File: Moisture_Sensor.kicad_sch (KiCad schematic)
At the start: 18 parts, among them J1 UPDI, J2 OLED SSD1306 0.96in, J3 STEMMA QT soil sensor, J4 Analog cap. sensor (alt), Q1 DMG3415U, SW1 READ, U1 ATtiny1614-SSNR, U2 TPS22917DBVR

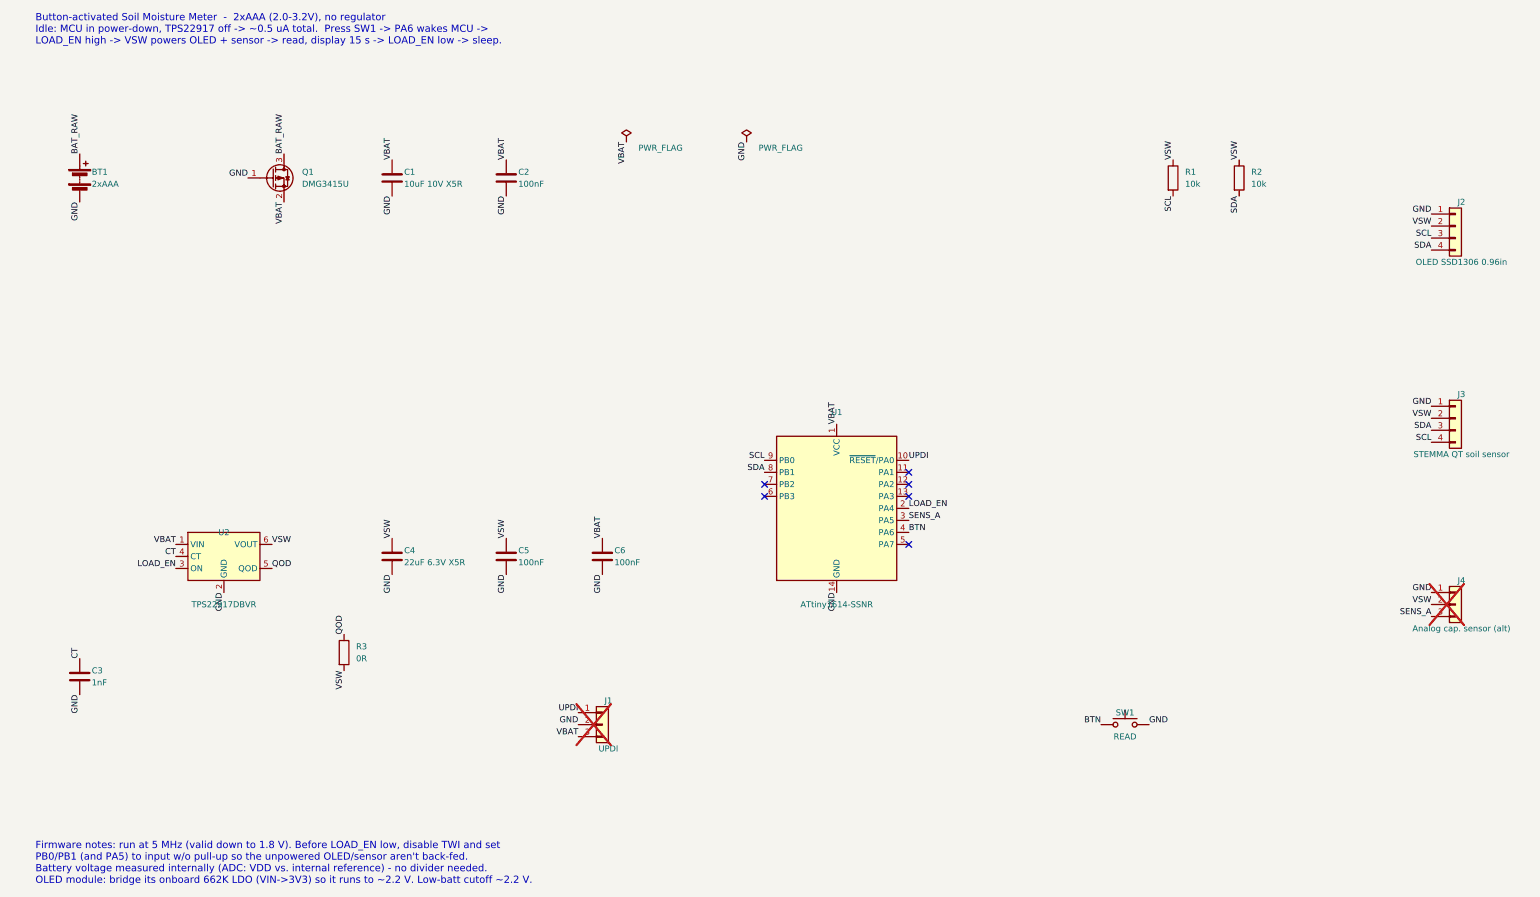
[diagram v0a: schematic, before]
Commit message: Add 25x17 mm PCB layout, STEP, renders; update schematic connectors
Co-authored-by: Copilot App <223556219+Copilot@users.noreply.github.com>
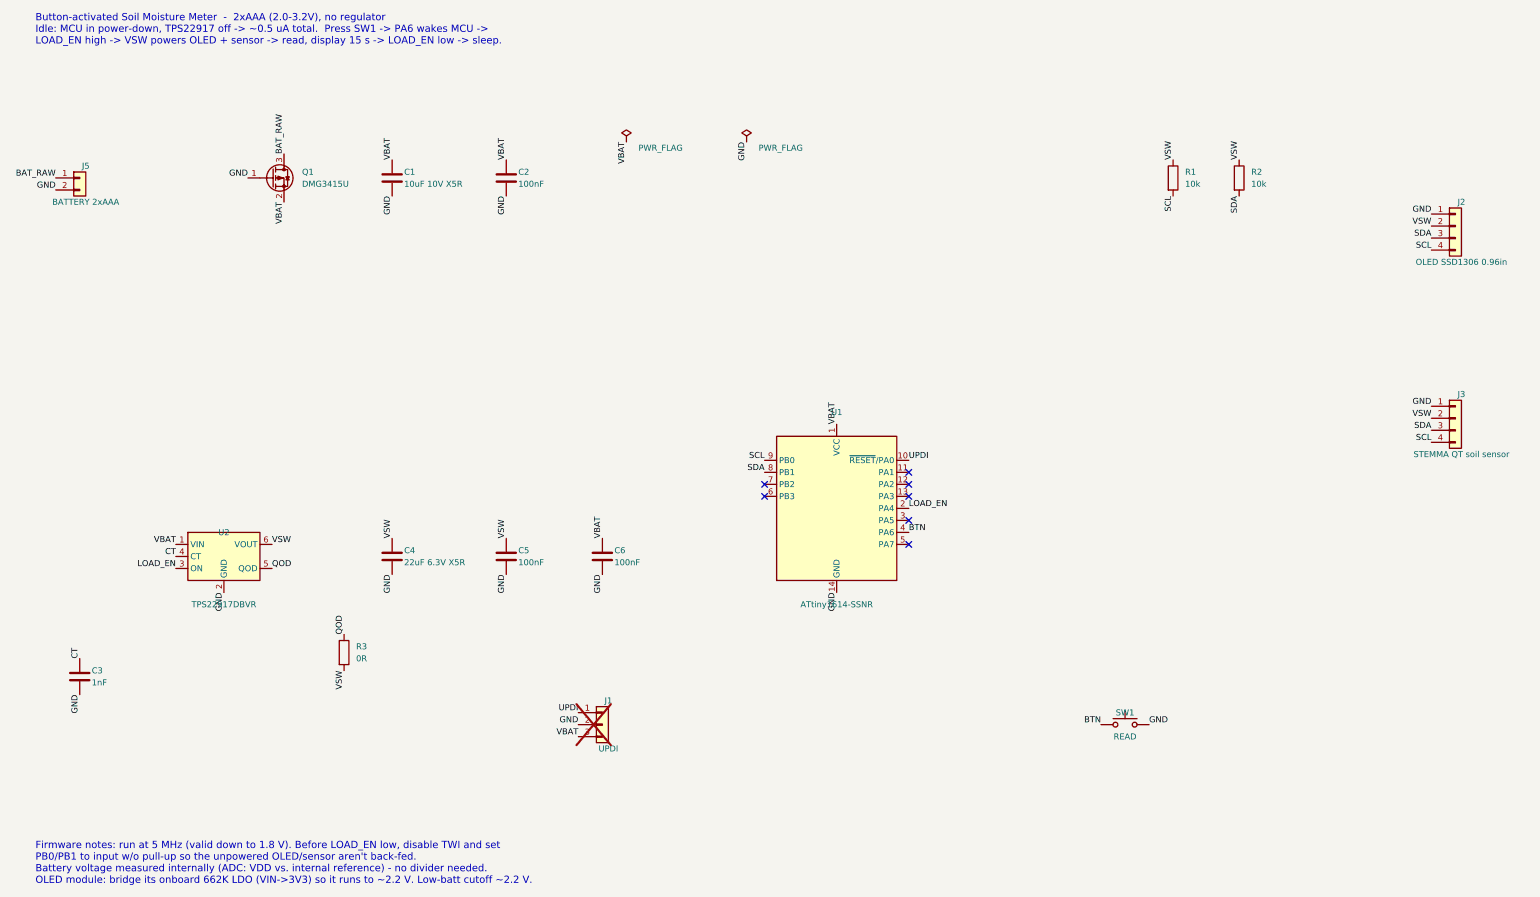
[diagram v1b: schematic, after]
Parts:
- removed BT1: 2xAAA, Battery:BatteryHolder_Keystone_2468_2xAAA, symbol Device:Battery
- removed J4: Analog cap. sensor (alt), Connector_JST:JST_PH_B3B-PH-K_1x03_P2.00mm_Vertical, symbol Connector_Generic:Conn_01x03
- added J5: BATTERY 2xAAA, Connector_JST:JST_PH_B2B-PH-K_1x02_P2.00mm_Vertical, symbol Connector_Generic:Conn_01x02
- J1: footprint Connector_PinHeader_2.54mm:PinHeader_1x03_P2.54mm_Vertical -> Connector_PinHeader_2.54mm:PinHeader_1x03_P2.54mm_Vertical_SMD_Pin1Left; Note Programming header (pogo pads / temporary header) -> UPDI programming pads on PCB bottom (pogo / temporary heade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
- J2: footprint Connector_PinHeader_2.54mm:PinHeader_1x04_P2.54mm_Vertical -> Connector_JST:JST_SH_SM04B-SRSS-TB_1x04-1MP_P1.00mm_Horizontal; MPN (none) -> SM04B-SRSS-TB(LF)(SN); Manufacturer (none) -> JST; Note ELEGOO 0.96in I2C OLED (GND,VCC,SCL,SDA) -> STEMMA QT pinout; cable e.g. Adafruit 4397 to OLED header
- SW1: footprint Button_Switch_THT:SW_PUSH_6mm -> Button_Switch_SMD:SW_Push_1P1T_NO_CK_KMR2; MPN B3F-1000 -> KMR221GLFS; Manufacturer Omron -> C&K
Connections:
- net BAT_RAW: now also J5.1 (Pin_1)
- net GND: now also J5.2 (Pin_2)
- net SCL: now also J2.4 (Pin_4); no longer J2.3 (Pin_3)
- net SDA: now also J2.3 (Pin_3); no longer J2.4 (Pin_4)
- net SENS_A: no longer names the net of U1.3 (PA5)
- no-connect marks 6 -> 7
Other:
- note added: "Firmware notes: run at 5 MHz (valid down to 1.8 V). Before LOAD_EN low, disable TWI and set PB0/PB1 to input w/o pull-up so the unpowered OLED/sensor aren't back-fed. Battery voltage measured internally (ADC: VDD vs. internal reference) - no divider needed. OLED module: bridge its onboard 662K LDO (VIN->3V3) so it runs to ~2.2 V. Low-batt cutoff ~2.2 V."
- note removed: "Firmware notes: run at 5 MHz (valid down to 1.8 V). Before LOAD_EN low, disable TWI and set PB0/PB1 (and PA5) to input w/o pull-up so the unpowered OLED/sensor aren't back-fed. Battery voltage measured internally (ADC: VDD vs. internal reference) - no divider needed. OLED module: bridge its onboard 662K LDO (VIN->3V3) so it runs to ~2.2 V. Low-batt cutoff ~2.2 V."
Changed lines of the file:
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@@
 	)
 	(symbol
-		(lib_id "Device:Battery")
+		(lib_id "Connector_Generic:Conn_01x02")
 		(at 39.37 59.69 0)
 		(unit 1)
@@
 		(on_board yes)
 		(dnp no)
-		(property "Reference" "BT1"
-			(at 41.91 58.42 0)
-			(effects
-				(font
-					(size 1.27 1.27)
-				)
-				(justify left)
-			)
-		)
-		(property "Value" "2xAAA"
-			(at 41.91 60.96 0)
-			(effects
-				(font
-					(size 1.27 1.27)
-				)
-				(justify left)
-			)
-		)
-		(property "Footprint" "Battery:BatteryHolder_Keystone_2468_2xAAA"
+		(property "Reference" "J5"
+			(at 40.64 57.15 0)
+			(effects
+				(font
+					(size 1.27 1.27)
+				)
+			)
+		)
+		(property "Value" "BATTERY 2xAAA"
+			(at 40.64 64.77 0)
+			(effects
+				(font
+					(size 1.27 1.27)
+				)
+			)
+		)
+		(property "Footprint" "Connector_JST:JST_PH_B2B-PH-K_1x02_P2.00mm_Vertical"
 			(at 39.37 59.69 0)
 			(hide yes)
@@
 			)
 		)
-		(property "MPN" "2468"
+		(property "MPN" "B2B-PH-K-S(LF)(SN)"
 			(at 39.37 59.69 0)
 			(hide yes)
@@
 			)
 		)
-		(property "Manufacturer" "Keystone"
+		(property "Manufacturer" "JST"
+			(at 39.37 59.69 0)
+			(hide yes)
+			(effects
+				(font
+					(size 1.27 1.27)
+				)
+			)
+		)
+		(property "Note" "2xAAA holder with JST-PH leads, in case (pin1 = +)"
 			(at 39.37 59.69 0)
 			(hide yes)
@@
 			(project "Moisture_Sensor"
 				(path "/0e800fc4-907d-5dc6-8843-971325c920e2"
-					(reference "BT1")
+					(reference "J5")
 					(unit 1)
 				)
@@
 	)
 	(label "BAT_RAW"
-		(at 39.37 54.61 90)
-		(effects
-			(font
-				(size 1.27 1.27)
-			)
-			(justify left bottom)
+		(at 34.29 59.69 180)
+		(effects
+			(font
+				(size 1.27 1.27)
+			)
+			(justify right bottom)
 		)
 	)
 	(label "GND"
-		(at 39.37 64.77 270)
+		(at 34.29 62.23 180)
 		(effects
 			(font
@@
 		)
 	)
-	(label "SENS_A"
-		(at 214.63 132.08 0)
-		(effects
-			(font
-				(size 1.27 1.27)
-			)
-			(justify left bottom)
-		)
+	(no_connect
+		(at 214.63 132.08)
 	)
 	(label "BTN"
@@
 			)
 		)
-		(property "Footprint" "Connector_PinHeader_2.54mm:PinHeader_1x03_P2.54mm_Vertical"
+		(property "Footprint" "Connector_PinHeader_2.54mm:PinHeader_1x03_P2.54mm_Vertical_SMD_Pin1Left"
 			(at 149.86 175.26 0)
 			(hide yes)
@@
 			)
 		)
-		(property "Note" "Programming header (pogo pads / temporary header)"
+		(property "Note" "UPDI programming pads on PCB bottom (pogo / temporary header)"
 			(at 149.86 175.26 0)
 			(hide yes)
@@
 			)
 		)
-		(property "Footprint" "Button_Switch_THT:SW_PUSH_6mm"
+		(property "Footprint" "Button_Switch_SMD:SW_Push_1P1T_NO_CK_KMR2"
 			(at 260.35 175.26 0)
 			(hide yes)
@@
 			)
 		)
-		(property "MPN" "B3F-1000"
+		(property "MPN" "KMR221GLFS"
 			(at 260.35 175.26 0)
 			(hide yes)
@@
 			)
 		)
-		(property "Manufacturer" "Omron"
+		(property "Manufacturer" "C&K"
 			(at 260.35 175.26 0)
 			(hide yes)
@@
 			)
 		)
-		(property "Footprint" "Connector_PinHeader_2.54mm:PinHeader_1x04_P2.54mm_Vertical"
+		(property "Footprint" "Connector_JST:JST_SH_SM04B-SRSS-TB_1x04-1MP_P1.00mm_Horizontal"
 			(at 330.2 69.85 0)
 			(hide yes)
@@
 			)
 		)
-		(property "Note" "ELEGOO 0.96in I2C OLED (GND,VCC,SCL,SDA)"
+		(property "MPN" "SM04B-SRSS-TB(LF)(SN)"
+			(at 330.2 69.85 0)
+			(hide yes)
+			(effects
+				(font
+					(size 1.27 1.27)
+				)
+			)
+		)
+		(property "Manufacturer" "JST"
+			(at 330.2 69.85 0)
+			(hide yes)
+			(effects
+				(font
+					(size 1.27 1.27)
+				)
+			)
+		)
+		(property "Note" "STEMMA QT pinout; cable e.g. Adafruit 4397 to OLED header"
 			(at 330.2 69.85 0)
 			(hide yes)
@@
 		)
 	)
+	(label "SDA"
+		(at 325.12 72.39 180)
+		(effects
+			(font
+				(size 1.27 1.27)
+			)
+			(justify right bottom)
+		)
+	)
 	(label "SCL"
-		(at 325.12 72.39 180)
-		(effects
-			(font
-				(size 1.27 1.27)
-			)
-			(justify right bottom)
-		)
-	)
-	(label "SDA"
 		(at 325.12 74.93 180)
 		(effects
@@
 		)
 	)
-	(symbol
-		(lib_id "Connector_Generic:Conn_01x03")
-		(at 330.2 149.86 0)
-		(unit 1)
-		(exclude_from_sim no)
-		(in_bom yes)
-		(on_board yes)
-		(dnp yes)
-		(property "Reference" "J4"
-			(at 331.47 144.78 0)
-			(effects
-				(font
-					(size 1.27 1.27)
-				)
-			)
-		)
-		(property "Value" "Analog cap. sensor (alt)"
-			(at 331.47 154.94 0)
-			(effects
-				(font
-					(size 1.27 1.27)
-				)
-			)
-		)
-		(property "Footprint" "Connector_JST:JST_PH_B3B-PH-K_1x03_P2.00mm_Vertical"
-			(at 330.2 149.86 0)
-			(hide yes)
-			(effects
-				(font
-					(size 1.27 1.27)
-				)
-			)
-		)
-		(property "Datasheet" ""
-			(at 330.2 149.86 0)
-			(hide yes)
-			(effects
-				(font
-					(size 1.27 1.27)
-				)
-			)
-		)
-		(property "MPN" "B3B-PH-K-S(LF)(SN)"
-			(at 330.2 149.86 0)
-			(hide yes)
-			(effects
-				(font
-					(size 1.27 1.27)
-				)
-			)
-		)
-		(property "Manufacturer" "JST"
-			(at 330.2 149.86 0)
-			(hide yes)
-			(effects
-				(font
-					(size 1.27 1.27)
-				)
-			)
-		)
-		(property "Note" "Optional: generic v1.2/v2.0 sensor, TLC555 version only"
-			(at 330.2 149.86 0)
-			(hide yes)
-			(effects
-				(font
-					(size 1.27 1.27)
-				)
-			)
-		)
-		(pin "1"
-		)
-		(pin "2"
-		)
-		(pin "3"
-		)
-		(instances
-			(project "Moisture_Sensor"
-				(path "/0e800fc4-907d-5dc6-8843-971325c920e2"
-					(reference "J4")
-					(unit 1)
-				)
-			)
-		)
-	)
-	(label "GND"
-		(at 325.12 147.32 180)
-		(effects
-			(font
-				(size 1.27 1.27)
-			)
-			(justify right bottom)
-		)
-	)
-	(label "VSW"
-		(at 325.12 149.86 180)
-		(effects
-			(font
-				(size 1.27 1.27)
-			)
-			(justify right bottom)
-		)
-	)
-	(label "SENS_A"
-		(at 325.12 152.4 180)
-		(effects
-			(font
-				(size 1.27 1.27)
-			)
-			(justify right bottom)
-		)
-	)
 	(text "Button-activated Soil Moisture Meter  -  2xAAA (2.0-3.2V), no regulator\nIdle: MCU in power-down, TPS22917 off -> ~0.5 uA total.  Press SW1 -> PA6 wakes MCU ->\nLOAD_EN high -> VSW powers OLED + sensor -> read, display 15 s -> LOAD_EN low -> sleep."
 		(exclude_from_sim no)
@@
 		)
 	)
-	(text "Firmware notes: run at 5 MHz (valid down to 1.8 V). Before LOAD_EN low, disable TWI and set\nPB0/PB1 (and PA5) to input w/o pull-up so the unpowered OLED/sensor aren't back-fed.\nBattery voltage measured internally (ADC: VDD vs. internal reference) - no divider needed.\nOLED module: bridge its onboard 662K LDO (VIN->3V3) so it runs to ~2.2 V. Low-batt cutoff ~2.2 V."
+	(text "Firmware notes: run at 5 MHz (valid down to 1.8 V). Before LOAD_EN low, disable TWI and set\nPB0/PB1 to input w/o pull-up so the unpowered OLED/sensor aren't back-fed.\nBattery voltage measured internally (ADC: VDD vs. internal reference) - no divider needed.\nOLED module: bridge its onboard 662K LDO (VIN->3V3) so it runs to ~2.2 V. Low-batt cutoff ~2.2 V."
 		(exclude_from_sim no)
 		(at 30 200 0)

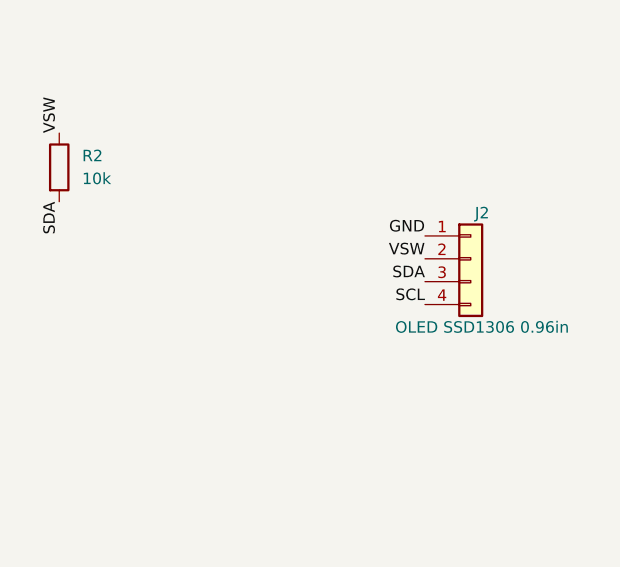
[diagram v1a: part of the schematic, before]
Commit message: Switch OLED connection to 2.54 mm pads matching ELEGOO module (GND-VCC-SCL-SDA)
Co-authored-by: Copilot App <223556219+Copilot@users.noreply.github.com>
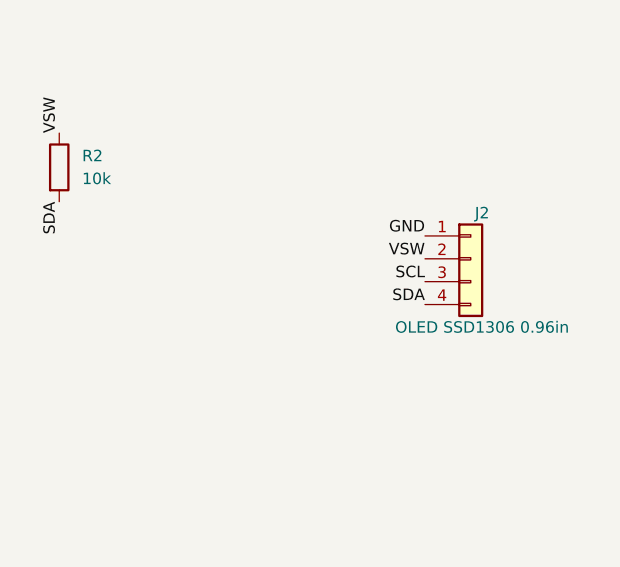
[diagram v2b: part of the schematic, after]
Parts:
- J2: footprint Connector_JST:JST_SH_SM04B-SRSS-TB_1x04-1MP_P1.00mm_Horizontal -> Connector_PinHeader_2.54mm:PinHeader_1x04_P2.54mm_Vertical; MPN SM04B-SRSS-TB(LF)(SN) -> Supplied Dupont wires soldered to pads (opt. 1x04 2.54mm he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; Manufacturer JST -> -; Note STEMMA QT pinout; cable e.g. Adafruit 4397 to OLED header -> ELEGOO 0.96in SSD1306 module, pin order GND-VCC-SCL-SDA
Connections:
- net SCL: now also J2.3 (Pin_3); no longer J2.4 (Pin_4)
- net SDA: now also J2.4 (Pin_4); no longer J2.3 (Pin_3)
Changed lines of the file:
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@@
 			)
 		)
-		(property "Footprint" "Connector_JST:JST_SH_SM04B-SRSS-TB_1x04-1MP_P1.00mm_Horizontal"
+		(property "Footprint" "Connector_PinHeader_2.54mm:PinHeader_1x04_P2.54mm_Vertical"
 			(at 330.2 69.85 0)
 			(hide yes)
@@
 			)
 		)
-		(property "MPN" "SM04B-SRSS-TB(LF)(SN)"
+		(property "MPN" "Supplied Dupont wires soldered to pads (opt. 1x04 2.54mm header)"
 			(at 330.2 69.85 0)
 			(hide yes)
@@
 			)
 		)
-		(property "Manufacturer" "JST"
+		(property "Manufacturer" "-"
 			(at 330.2 69.85 0)
 			(hide yes)
@@
 			)
 		)
-		(property "Note" "STEMMA QT pinout; cable e.g. Adafruit 4397 to OLED header"
+		(property "Note" "ELEGOO 0.96in SSD1306 module, pin order GND-VCC-SCL-SDA"
 			(at 330.2 69.85 0)
 			(hide yes)
@@
 		)
 	)
-	(label "SDA"
+	(label "SCL"
 		(at 325.12 72.39 180)
 		(effects
@@
 		)
 	)
-	(label "SCL"
+	(label "SDA"
 		(at 325.12 74.93 180)
 		(effects
